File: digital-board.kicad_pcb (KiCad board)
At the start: 2 copper layers, 200 x 150 mm, 241 parts, among them IC1 ATMEGA6450-A, J1 CONN_20X2, Q1 2N3904, Q2 2N3904, SW15 TACT_SWITCH, SW16 TACT_SWITCH, SW17 TACT_SWITCH, SW18 TACT_SWITCH, SW19 TACT_SWITCH, SW20 TACT_SWITCH, SW21 TACT_SWITCH, SW22 TACT_SWITCH, SW23 TACT_SWITCH, U1 DG419, U10 74LVC1G32, U11 74HC165, U12 74AC595, U13 74AC595, U14 74HC165, U15 74AC595, U16 74AC595, U2 74HC4067, U3 R-78E5.0-1.0, U4 74HC4067, U5 74LS573, U6 74LS573, U7 74LVC2G04, U8 74AC595, U9 74HC165, X1 MIDI OUT, X2 MIDI IN, X3 MIDI THRU

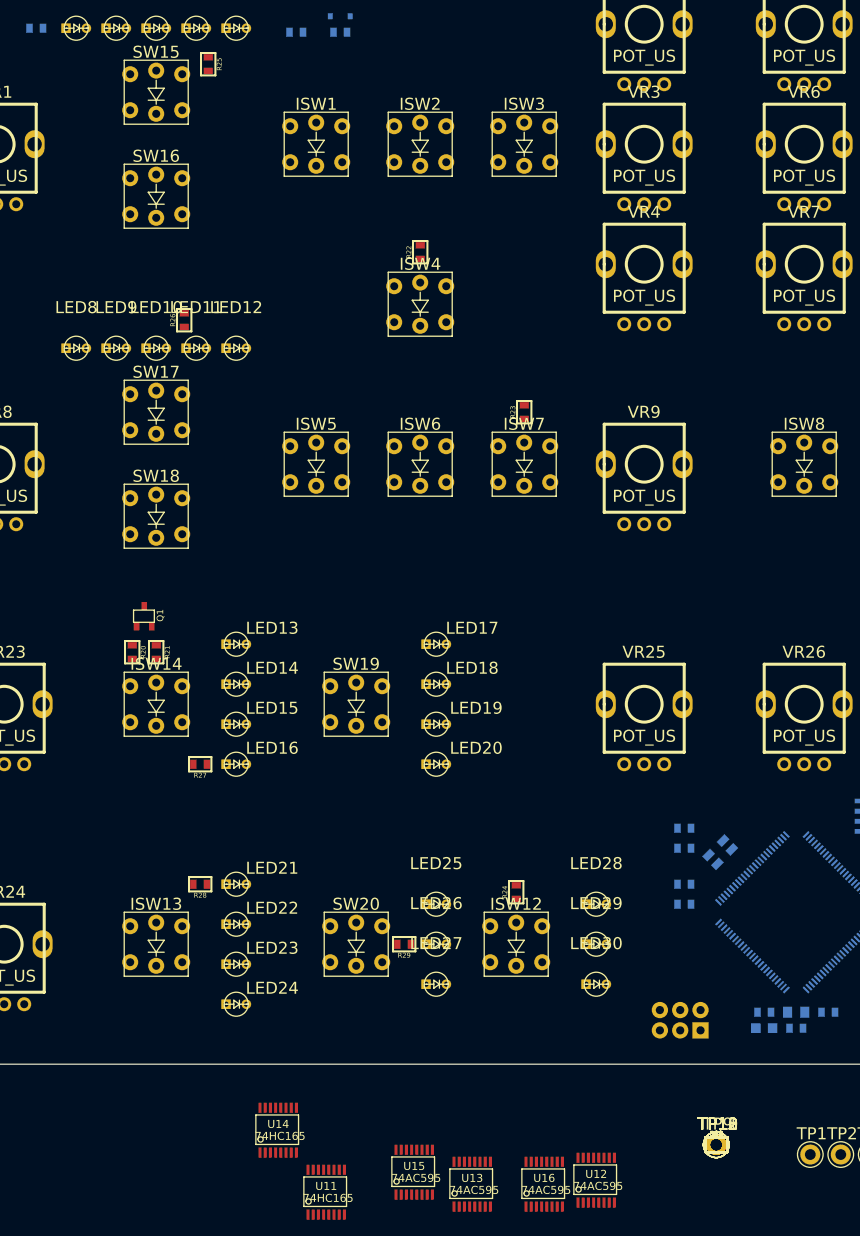
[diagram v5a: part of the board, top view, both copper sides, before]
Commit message: led driver layout
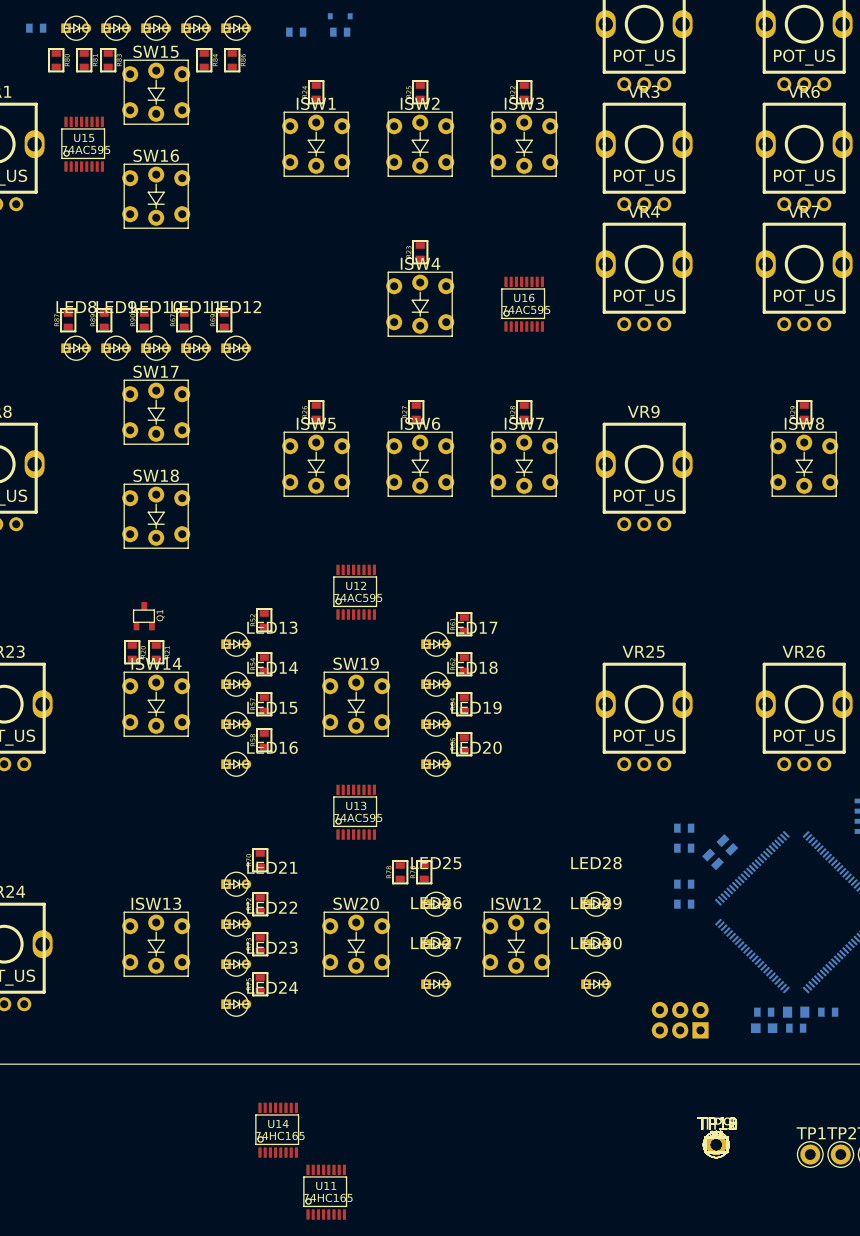
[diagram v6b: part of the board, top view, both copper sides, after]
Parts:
- moved R80 158.7 mm to (17.5, 24.5), turned to 270 degrees
- moved R81 156.9 mm to (21.0, 24.5), turned to 270 degrees
- moved R83 155.4 mm to (24.0, 24.5), turned to 270 degrees
- moved R84 149.9 mm to (36.0, 24.5), turned to 270 degrees
- moved R86 148.5 mm to (39.5, 24.5), turned to 270 degrees
- moved U15 135.0 mm to (21.0, 35.0)
- moved R87 131.1 mm to (19.0, 57.0), turned to 90 degrees
- moved R89 128.4 mm to (23.5, 57.0), turned to 90 degrees
- moved R90 125.4 mm to (28.5, 57.0), turned to 90 degrees
- moved R67 122.7 mm to (33.5, 57.0), turned to 90 degrees
- moved R69 120.0 mm to (38.5, 57.0), turned to 90 degrees
- moved U16 110.0 mm to (76.0, 55.0)
- moved R24 103.1 mm to (50.0, 28.5)
- moved R52 86.6 mm to (43.5, 94.5), turned to 90 degrees
- moved R29 83.2 mm to (111.0, 68.5), turned to 90 degrees
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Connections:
- R22 pad 1: Net-(ISW1-Pad6) -> Net-(ISW3-Pad6)
- R23 pad 1: Net-(ISW2-Pad6) -> Net-(ISW4-Pad6)
- R24 pad 1: Net-(ISW3-Pad6) -> Net-(ISW1-Pad6)
- R25 pad 1: Net-(ISW4-Pad6) -> Net-(ISW2-Pad6)
- U13 pad 6: Net-(R76-Pad2) -> Net-(R78-Pad2)
- U13 pad 7: Net-(R78-Pad2) -> Net-(R76-Pad2)
- U15 pad 1: Net-(R81-Pad2) -> Net-(R80-Pad2)
- U15 pad 15: Net-(R80-Pad2) -> Net-(R83-Pad2)
- U15 pad 2: Net-(R83-Pad2) -> Net-(R81-Pad2)

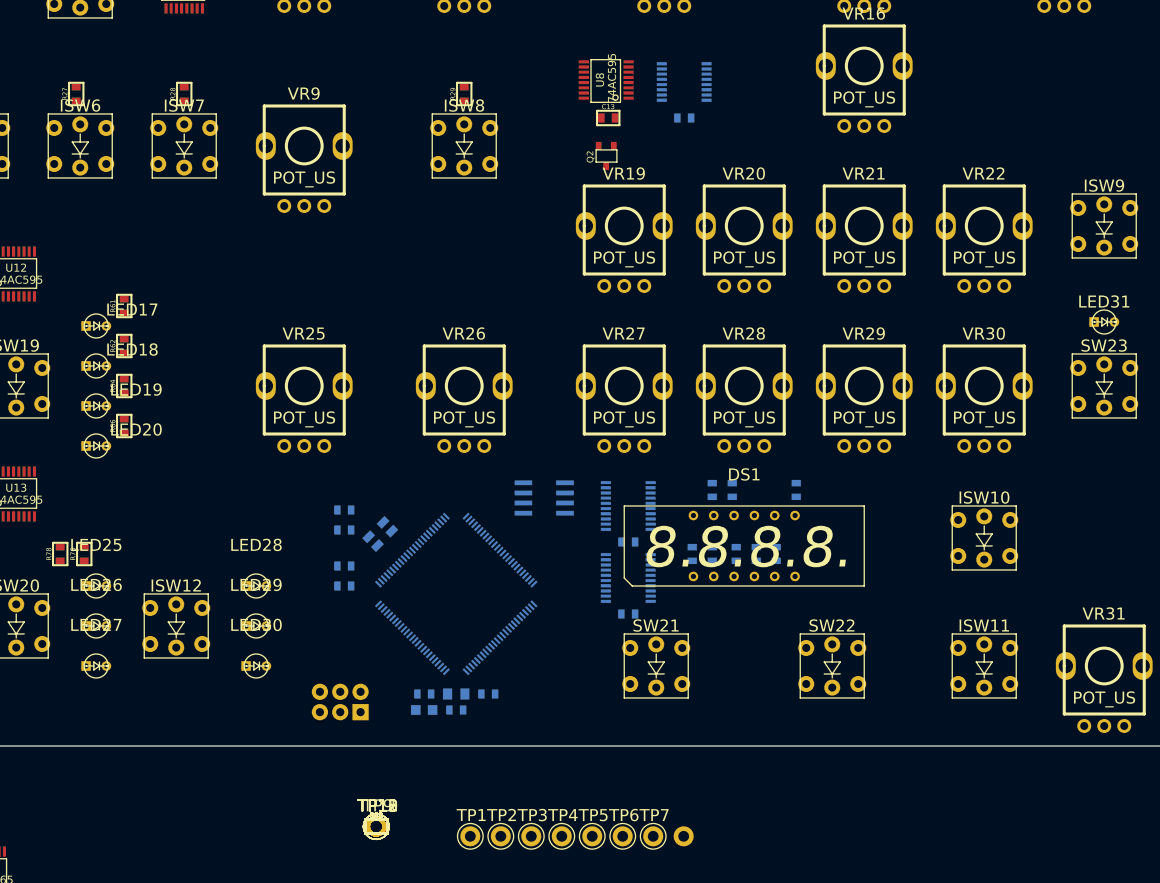
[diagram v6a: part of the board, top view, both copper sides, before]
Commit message: LED array layout
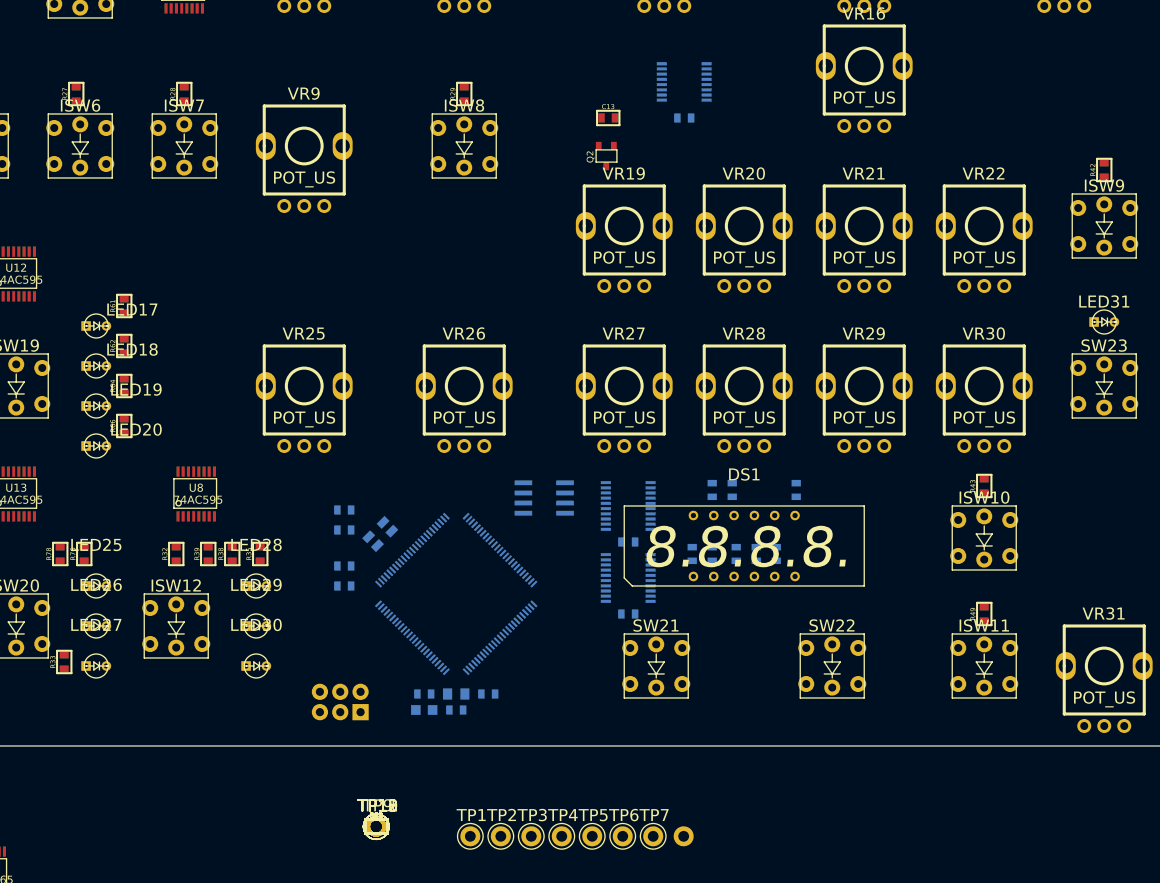
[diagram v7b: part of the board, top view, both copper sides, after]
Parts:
- moved R42 122.5 mm to (191.0, 78.0), turned to 90 degrees
- moved R43 87.1 mm to (176.0, 117.5), turned to 90 degrees
- moved R49 80.5 mm to (176.0, 133.5), turned to 90 degrees
- moved U8 72.8 mm to (77.5, 118.5), turned to 0 degrees
- moved R33 44.1 mm to (61.0, 139.5), turned to 90 degrees
- moved R32 42.3 mm to (75.0, 126.0), turned to 90 degrees
- moved R39 40.0 mm to (79.0, 126.0), turned to 90 degrees
- moved R38 38.5 mm to (82.0, 126.0), turned to 90 degrees
- moved R35 37.0 mm to (85.5, 126.0), turned to 90 degrees
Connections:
- U8 pad 15: Net-(R32-Pad2) -> Net-(R42-Pad2)
- U8 pad 2: Net-(R35-Pad2) -> Net-(R32-Pad2)
- U8 pad 3: Net-(R38-Pad2) -> Net-(R39-Pad2)
- U8 pad 4: Net-(R39-Pad2) -> Net-(R38-Pad2)
- U8 pad 5: Net-(R42-Pad2) -> Net-(R35-Pad2)
